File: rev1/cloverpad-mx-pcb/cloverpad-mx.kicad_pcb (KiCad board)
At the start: 2 copper layers, 70 x 75 mm, 42 parts, among them J1 USB_C_Receptacle_USB2.0, SW1 SW_Push, SW2 SW_Push, U1 SRV05-4, U2 XC6206P332MR, U8 RP2040, U9 W25Q16JVSSIQ, Y1 12MHz

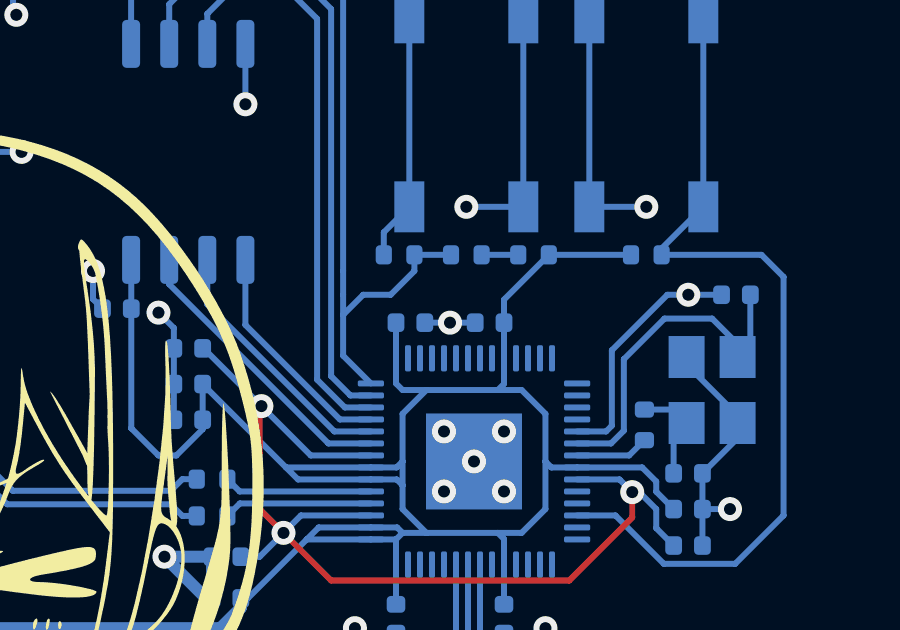
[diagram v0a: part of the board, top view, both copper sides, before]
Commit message: chore: update all symbols + footprints to match kicad 8
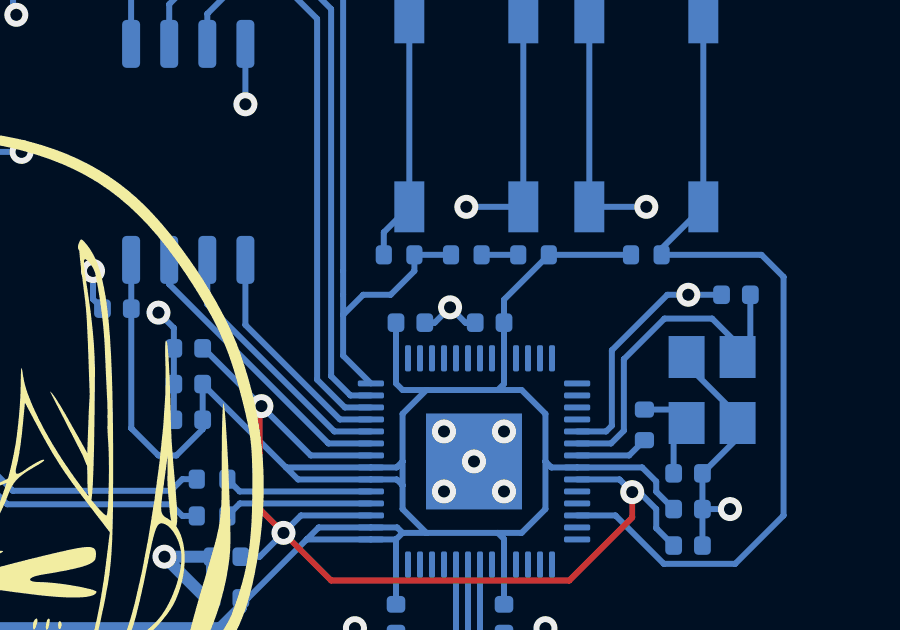
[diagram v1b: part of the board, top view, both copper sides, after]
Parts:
- MX1, MX2, MX3: footprint PCM_marbastlib-mx:SW_MX_HS_1u -> PCM_marbastlib-mx:SW_MX_HS_CPG151101S11_1u
